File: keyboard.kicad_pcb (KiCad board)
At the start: 2 copper layers, 305.7 x 121 mm, 172 parts, among them J1 Conn_02x20_Odd_Even, J2 USB_C_Receptacle

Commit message: feat: change the pin socket to 2.54mm
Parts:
- J1: footprint Connector_PinSocket_1.27mm:PinSocket_2x20_P1.27mm_Vertical_SMD -> Connector_PinSocket_2.54mm:PinSocket_2x20_P2.54mm_Vertical_SMD
- moved D-67 24.3 mm to (345.5, 80.2), turned to 90 degrees
- moved J1 16.7 mm to (306.2, 89.1)
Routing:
- net /RX_N: track 64.1 -> 32.9 mm, vias 4 -> 1
- net COL13: track 197.4 -> 167.1 mm
- net COL15: track 183.7 -> 154.3 mm
- net SCLK: track 63.1 -> 34.6 mm
- net COL14: track 165.3 -> 138.3 mm
- net CAPS: track 37.4 -> 10.8 mm
- net Net-(D-67-Pad2): track 19.3 -> 45.3 mm
- net COL11: track 159.0 -> 184.1 mm, vias 2 -> 1
- net COL9: track 169.0 -> 191.9 mm, vias 2 -> 1
- net COL10: track 156.4 -> 178.5 mm
- net COL8: track 187.3 -> 208.4 mm, vias 2 -> 1
- net /CC1: track 17.1 -> 37.1 mm
- net /TX_P: track 30.2 -> 50.2 mm, vias 2 -> 1
- net ROW1: track 302.9 -> 320.0 mm
- net COL12: track 161.8 -> 178.5 mm, vias 4 -> 1
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
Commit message: feat: add battery indicator and change the pin socket layout
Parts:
- added D3: D, LED_SMD:LED_0603_1608Metric, F.Cu at (70.5, 89.3)
- added D4: D, LED_SMD:LED_0603_1608Metric, F.Cu at (73.6, 89.3)
- added D5: D, LED_SMD:LED_0603_1608Metric, F.Cu at (76.7, 89.3)
- moved J1 29.5 mm to (276.7, 89.4)
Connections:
- J1 pad 2: GND -> /L3
- J1 pad 20: /RX_N -> GND
- J1 pad 22: /RX_P -> GND
- J1 pad 24: /TX_N -> GND
- J1 pad 26: /TX_P -> GND
- J1 pad 28: /CC2 -> VBUS
- J1 pad 30: /CC1 -> /USBD_P
- J1 pad 34: /USBD_P -> GND
- J1 pad 4: VBUS -> /L2
- J1 pad 6: GND -> /L1
- J2 pad A10: /RX_N -> (no net)
- J2 pad A11: /RX_P -> (no net)
- J2 pad A2: /TX_P -> (no net)
- J2 pad A3: /TX_N -> (no net)
- J2 pad A5: /CC1 -> (no net)
- J2 pad A8: GND -> (no net)
- J2 pad B10: /RX_N -> (no net)
- J2 pad B11: /RX_P -> (no net)
- J2 pad B2: /TX_P -> (no net)
- J2 pad B3: /TX_N -> (no net)
- J2 pad B5: /CC2 -> (no net)
- J2 pad B8: GND -> (no net)
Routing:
- net ROW6: track 381.7 -> 0.00 mm
- net ROW4: track 378.5 -> 0.00 mm
- net ROW5: track 361.9 -> 0.00 mm
- net COL1: track 346.0 -> 0.00 mm, vias 1 -> 0
- net COL2: track 340.9 -> 0.00 mm, vias 1 -> 0
- net COL3: track 324.7 -> 0.00 mm, vias 1 -> 0
- net ROW3: track 323.4 -> 0.00 mm
- net ROW1: track 320.0 -> 0.00 mm
- net COL4: track 305.1 -> 0.00 mm, vias 1 -> 0
- net ROW2: track 301.0 -> 0.00 mm
- net COL5: track 298.2 -> 0.00 mm, vias 1 -> 0
- net COL6: track 241.1 -> 0.00 mm, vias 1 -> 0
- net COL7: track 224.7 -> 0.00 mm, vias 1 -> 0
- net COL8: track 208.4 -> 0.00 mm, vias 1 -> 0
- net COL9: track 191.9 -> 0.00 mm, vias 1 -> 0
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
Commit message: fix: fix the pinsocket and pinheader config
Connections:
- J1 pad 8: GND -> (no net)
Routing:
- net ROW4: track 0.00 -> 426.1 mm
- net ROW6: track 0.00 -> 382.5 mm
- net GND: track 0.00 -> 376.4 mm
- net ROW5: track 0.00 -> 359.3 mm
- net ROW3: track 0.00 -> 319.5 mm
- net COL1: track 0.00 -> 319.3 mm, vias 0 -> 1
- net COL2: track 0.00 -> 311.3 mm, vias 0 -> 1
- net ROW1: track 0.00 -> 308.7 mm
- net ROW2: track 0.00 -> 299.4 mm
- net COL3: track 0.00 -> 294.7 mm, vias 0 -> 1
- net COL4: track 0.00 -> 276.7 mm, vias 0 -> 1
- net COL5: track 0.00 -> 269.0 mm, vias 0 -> 1
- net COL6: track 0.00 -> 211.9 mm, vias 0 -> 1
- net COL7: track 0.00 -> 194.6 mm, vias 0 -> 1
- net /L1: track 0.00 -> 189.5 mm, vias 0 -> 1
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
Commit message: feat: change the typec from 24 pin to 16 pin
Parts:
- J2: value USB_C_Receptacle -> USB_C_Receptacle_16P; footprint keyboard:USB_C_Receptacle -> keyboard:USB_C_Receptacle_16P
- moved J2 2.22 mm to (286.6, 71.6)
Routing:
- net ROW4: track 426.1 -> 0.00 mm
- net ROW6: track 382.5 -> 0.00 mm
- net GND: track 376.4 -> 0.00 mm
- net ROW5: track 359.3 -> 0.00 mm
- net ROW3: track 319.5 -> 0.00 mm
- net COL1: track 319.3 -> 0.00 mm, vias 1 -> 0
- net COL2: track 311.3 -> 0.00 mm, vias 1 -> 0
- net ROW1: track 308.7 -> 0.00 mm
- net ROW2: track 299.4 -> 0.00 mm
- net COL3: track 294.7 -> 0.00 mm, vias 1 -> 0
- net COL4: track 276.7 -> 0.00 mm, vias 1 -> 0
- net COL5: track 269.0 -> 0.00 mm, vias 1 -> 0
- net COL6: track 211.9 -> 0.00 mm, vias 1 -> 0
- net COL7: track 194.6 -> 0.00 mm, vias 1 -> 0
- net /L1: track 189.5 -> 0.00 mm, vias 1 -> 0
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
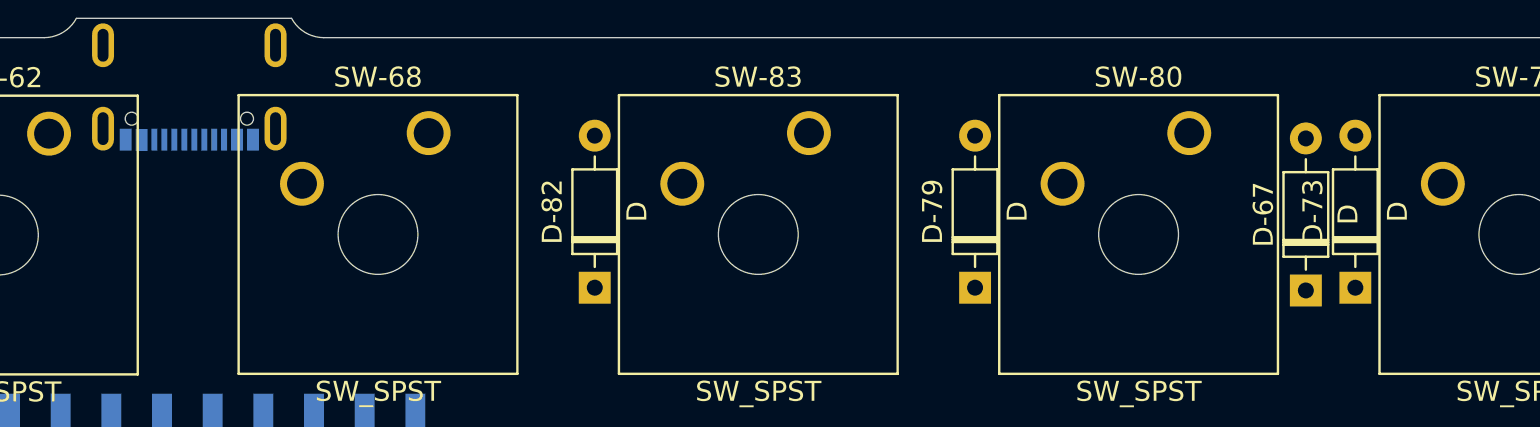
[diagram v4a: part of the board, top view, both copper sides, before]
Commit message: feat: update the typec footprint
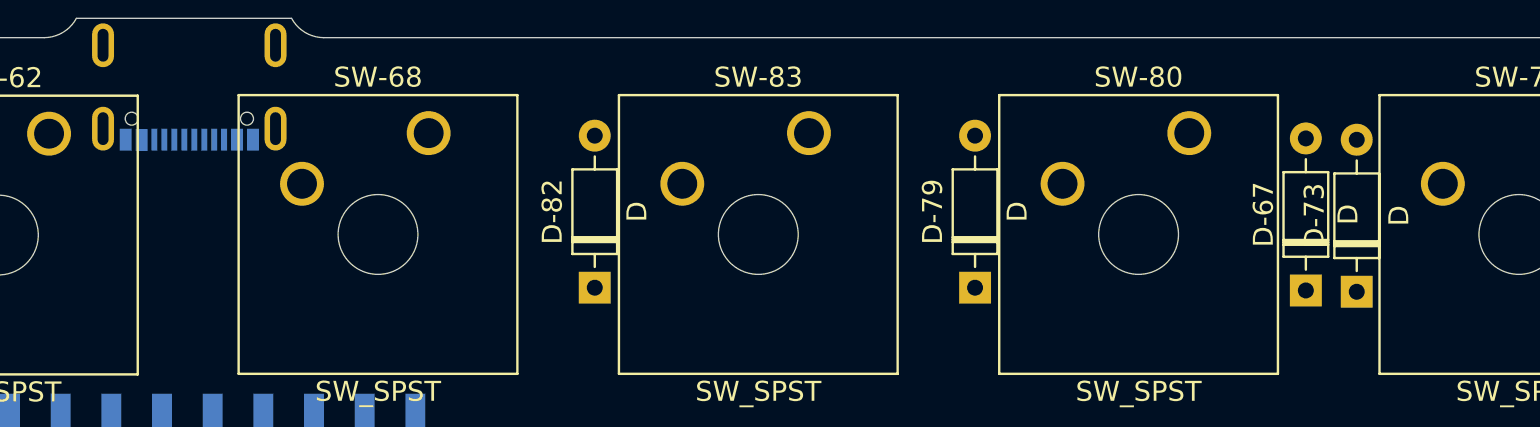
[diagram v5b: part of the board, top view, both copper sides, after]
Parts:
- moved D-73 0.21 mm to (348.0, 80.3)
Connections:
- J2 pad B6: /USBD_P -> (no net)
- J2 pad B7: /USBD_N -> (no net)
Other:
- rule via_min_size: 0.3 -> 0.1
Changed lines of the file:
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@@
-(kicad_pcb (version 20171130) (host pcbnew "(5.1.2-1)-1")
+(kicad_pcb (version 20171130) (host pcbnew "(5.1.5-0-10_14)")
   (general
     (thickness 1.6)
@@
   )
   (setup
-    (last_trace_width 0.25)
-    (user_trace_width 0.01)
+    (last_trace_width 0.2)
     (user_trace_width 0.2)
     (user_trace_width 0.298)
+    (user_trace_width 0.3)
     (user_trace_width 0.5953)
     (user_trace_width 1.191)
@@
     (via_size 0.8)
     (via_drill 0.4)
-    (via_min_size 0.3)
+    (via_min_size 0.1)
     (via_min_drill 0.3)
+    (user_via 0.4 0.3)
     (uvia_size 0.3)
     (uvia_drill 0.1)
     (uvias_allowed no)
-    (uvia_min_size 0.3)
+    (uvia_min_size 0.1)
     (uvia_min_drill 0.1)
     (edge_width 0.05)
@@
     (mod_text_size 1 1)
     (mod_text_width 0.15)
-    (pad_size 5 5)
-    (pad_drill 3.2)
+    (pad_size 0.3 1.1)
+    (pad_drill 0)
     (pad_to_mask_clearance 0.051)
     (solder_mask_min_width 0.25)
@@
     (add_net "Net-(D-9-Pad2)")
     (add_net "Net-(D-SPACE1-Pad2)")
-    (add_net "Net-(J2-PadA5)")
-    (add_net "Net-(J2-PadA8)")
-    (add_net "Net-(J2-PadB5)")
-    (add_net "Net-(J2-PadB8)")
     (add_net ROW1)
     (add_net ROW2)
@@
     (add_net SCLK)
     (add_net VBUS)
-    (add_net VDD33)
   )
   (module keyboard:USB_C_Receptacle_16P (layer B.Cu)
@@
     (pad S1 thru_hole oval (at 7.21 0.5) (size 1.1 2.2) (drill oval 0.55 1.65) (layers *.Cu *.Mask)
       (net 24 GND))
-    (pad A12 smd rect (at 6.23 1.05) (size 0.3 1.1) (layers B.Cu B.Paste B.Mask)
-      (net 24 GND))
-    (pad A9 smd rect (at 5.43 1.05) (size 0.3 1.1) (layers B.Cu B.Paste B.Mask)
-      (net 25 VBUS))
-    (pad A4 smd rect (at 0.348 1.07) (size 0.3 1.1) (layers B.Cu B.Paste B.Mask)
+    (pad A4 smd rect (at 0.498 1.07) (size 0.6 1.1) (layers B.Cu B.Paste B.Mask)
       (net 25 VBUS))
     (pad "" np_thru_hole circle (at 0 0) (size 0.65 0.65) (drill 0.65) (layers *.Cu *.Mask))
-    (pad B4 smd rect (at 5.131 1.05) (size 0.3 1.1) (layers B.Cu B.Paste B.Mask)
+    (pad B4 smd rect (at 5.281 1.05) (size 0.6 1.1) (layers B.Cu B.Paste B.Mask)
       (net 25 VBUS))
-    (pad B6 smd rect (at 3.637 1.05) (size 0.3 1.1) (layers B.Cu B.Paste B.Mask)
-      (net 26 /USBD_P))
+    (pad B6 smd rect (at 3.637 1.05) (size 0.3 1.1) (layers B.Cu B.Paste B.Mask))
     (pad A8 smd rect (at 4.135 1.05) (size 0.3 1.1) (layers B.Cu B.Paste B.Mask))
     (pad B5 smd rect (at 4.633 1.05) (size 0.3 1.1) (layers B.Cu B.Paste B.Mask))
-    (pad B1 smd rect (at 5.93 1.05) (size 0.3 1.1) (layers B.Cu B.Paste B.Mask)
+    (pad B1 smd rect (at 6.08 1.05) (size 0.6 1.1) (layers B.Cu B.Paste B.Mask)
       (net 24 GND))
     (pad A7 smd rect (at 3.139 1.05) (size 0.3 1.1) (layers B.Cu B.Paste B.Mask)
@@
     (pad A6 smd rect (at 2.641 1.05) (size 0.3 1.1) (layers B.Cu B.Paste B.Mask)
       (net 26 /USBD_P))
-    (pad B7 smd rect (at 2.134 1.05) (size 0.3 1.1) (layers B.Cu B.Paste B.Mask)
-      (net 27 /USBD_N))
+    (pad B7 smd rect (at 2.134 1.05) (size 0.3 1.1) (layers B.Cu B.Paste B.Mask))
     (pad A5 smd rect (at 1.636 1.05) (size 0.3 1.1) (layers B.Cu B.Paste B.Mask))
     (pad B8 smd rect (at 1.138 1.05) (size 0.3 1.1) (layers B.Cu B.Paste B.Mask))
-    (pad B9 smd rect (at 0.64 1.07) (size 0.3 1.1) (layers B.Cu B.Paste B.Mask)
-      (net 25 VBUS))
-    (pad A1 smd rect (at -0.45 1.05) (size 0.3 1.1) (layers B.Cu B.Paste B.Mask)
+    (pad A1 smd rect (at -0.3 1.05) (size 0.6 1.1) (layers B.Cu B.Paste B.Mask)
       (net 24 GND))
     (pad S1 thru_hole oval (at -1.435 0.5) (size 1.1 2.2) (drill oval 0.55 1.65) (layers *.Cu *.Mask)
       (net 24 GND))
     (pad "" np_thru_hole circle (at 5.78 0) (size 0.65 0.65) (drill 0.65) (layers *.Cu *.Mask))
-    (pad B12 smd rect (at -0.15 1.05) (size 0.3 1.1) (layers B.Cu B.Paste B.Mask)
-      (net 24 GND))
     (model ${KIPRJMOD}/keyboard.pretty/USB_C_Receptacle.step
       (offset (xyz -1.55 -6.2 0))
@@
   )
   (module keyboard:D_DO-35_SOD27_P7.62mm_Horizontal (layer F.Cu)
-    (at 347.94 80.052 90)
+    (at 348.01 80.255 90)
     (descr "Diode, DO-35_SOD27 series, Axial, Horizontal, pin pitch=7.62mm, , length*diameter=4*2mm^2, , http://www.diodes.com/_files/packages/DO-35.pdf")
     (tags "Diode DO-35_SOD27 series Axial Horizontal pin pitch 7.62mm  length 4mm diameter 2mm")

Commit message: feat: change global label to label
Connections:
- net CAPS renamed /CAPS
- net COL1 renamed /COL1
- net COL10 renamed /COL10
- net COL11 renamed /COL11
- net COL12 renamed /COL12
- net COL13 renamed /COL13
- net COL14 renamed /COL14
- net COL2 renamed /COL2
- net COL3 renamed /COL3
- net COL4 renamed /COL4
- net COL5 renamed /COL5
- net COL6 renamed /COL6
- net COL7 renamed /COL7
- net COL8 renamed /COL8
- net COL9 renamed /COL9
- net ROW1 renamed /ROW1
- net ROW2 renamed /ROW2
- net ROW3 renamed /ROW3
- net ROW4 renamed /ROW4
- net ROW5 renamed /ROW5
- net ROW6 renamed /ROW6
- net SCLK renamed /SCLK
- J1 pad 40: COL15 -> (no net)
- J2 pad B6: (no net) -> /USBD_P
- J2 pad B7: (no net) -> /USBD_N
- SW-80 pad 2: COL15 -> /COL15
- SW-81 pad 2: COL15 -> /COL15
- SW-82 pad 2: COL15 -> /COL15
- SW-83 pad 2: COL15 -> /COL15
- SW-84 pad 2: COL15 -> /COL15

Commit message: feat: update the jst package
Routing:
- net /USBD_N: track 0.00 -> 20.6 mm, vias 0 -> 2
- net /USBD_P: track 0.00 -> 19.8 mm

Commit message: feat: rerouting the cc and keyboard
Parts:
- moved J1 0.42 mm to (276.3, 89.4)
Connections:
- J1 pad 30: /USBD_P -> /USBD_N
- J1 pad 32: /USBD_N -> /USBD_P
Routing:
- net /ROW4: track 0.00 -> 427.1 mm
- net GND: track 0.00 -> 382.1 mm
- net /ROW6: track 0.00 -> 381.2 mm
- net /ROW5: track 0.00 -> 361.1 mm
- net /ROW3: track 0.00 -> 319.8 mm
- net /COL1: track 0.00 -> 316.2 mm, vias 0 -> 1
- net /COL2: track 0.00 -> 311.3 mm, vias 0 -> 1
- net /ROW1: track 0.00 -> 308.8 mm
- net /ROW2: track 0.00 -> 299.1 mm
- net /COL3: track 0.00 -> 294.4 mm, vias 0 -> 1
- net /COL4: track 0.00 -> 274.0 mm, vias 0 -> 1
- net /COL5: track 0.00 -> 268.8 mm, vias 0 -> 1
- net /COL6: track 0.00 -> 222.4 mm
- net /COL7: track 0.00 -> 207.9 mm
- net /COL11: track 0.00 -> 196.6 mm, vias 0 -> 1
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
